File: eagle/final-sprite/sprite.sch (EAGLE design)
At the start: 60 parts, among them J1 M20-7910442R, U1 CC430F513X, U2 LSM9DS1, U4 DRV8837, U5 ADP5092, U6 DRV8837, U7 DRV8837, X1 SPRITEPIN_SPRITE_PIN, X2 SPRITEPIN_SPRITE_PIN

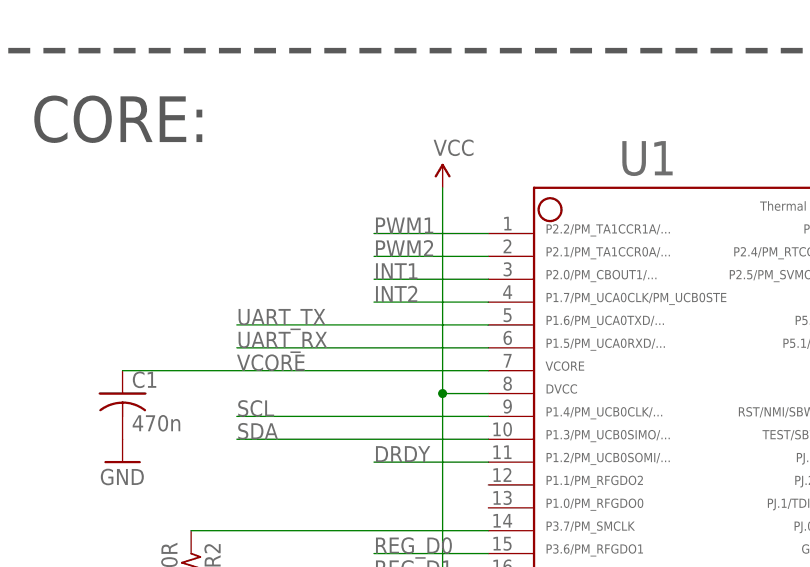
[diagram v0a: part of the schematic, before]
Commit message: routed some more routes
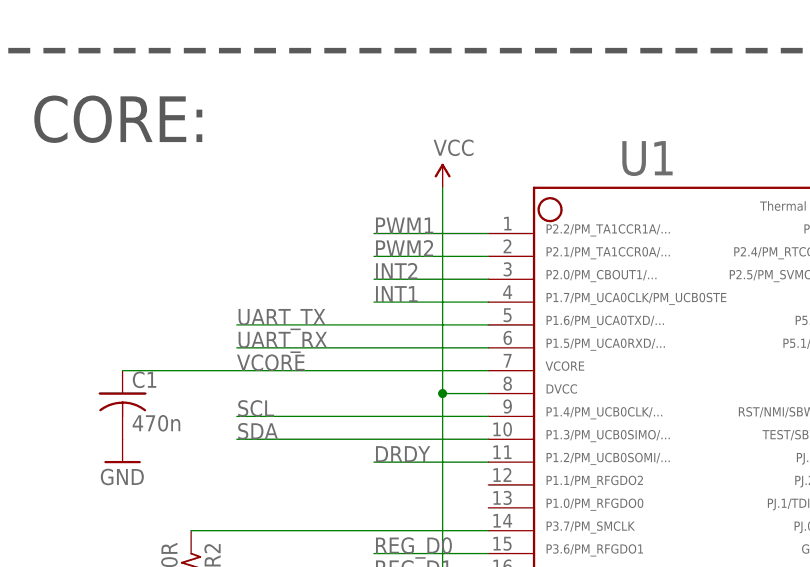
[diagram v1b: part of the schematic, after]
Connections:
- net INT1: now also U1.4; no longer U1.3
- net INT2: now also U1.3; no longer U1.4
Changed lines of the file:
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@@
 </segment>
 <segment>
-<wire x1="-20.32" y1="-193.04" x2="-33.02" y2="-193.04" width="0.1524" layer="91"/>
-<label x="-33.02" y="-193.04" size="1.778" layer="95"/>
-<pinref part="U1" gate="G$1" pin="3"/>
+<wire x1="-20.32" y1="-195.58" x2="-33.02" y2="-195.58" width="0.1524" layer="91"/>
+<label x="-33.02" y="-195.58" size="1.778" layer="95"/>
+<pinref part="U1" gate="G$1" pin="4"/>
 </segment>
 </net>
@@
 </segment>
 <segment>
-<wire x1="-20.32" y1="-195.58" x2="-33.02" y2="-195.58" width="0.1524" layer="91"/>
-<label x="-33.02" y="-195.58" size="1.778" layer="95"/>
-<pinref part="U1" gate="G$1" pin="4"/>
+<wire x1="-20.32" y1="-193.04" x2="-33.02" y2="-193.04" width="0.1524" layer="91"/>
+<label x="-33.02" y="-193.04" size="1.778" layer="95"/>
+<pinref part="U1" gate="G$1" pin="3"/>
 </segment>
 </net>

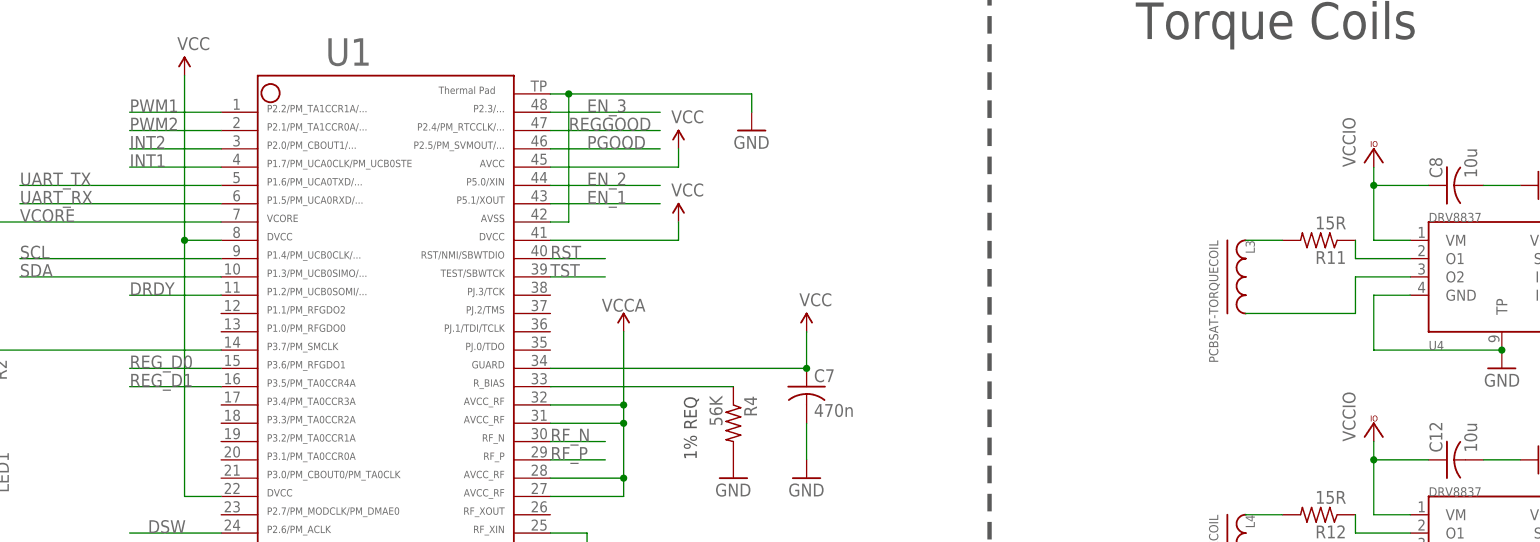
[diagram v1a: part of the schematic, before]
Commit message: routed all traces, need to do GND and VCC
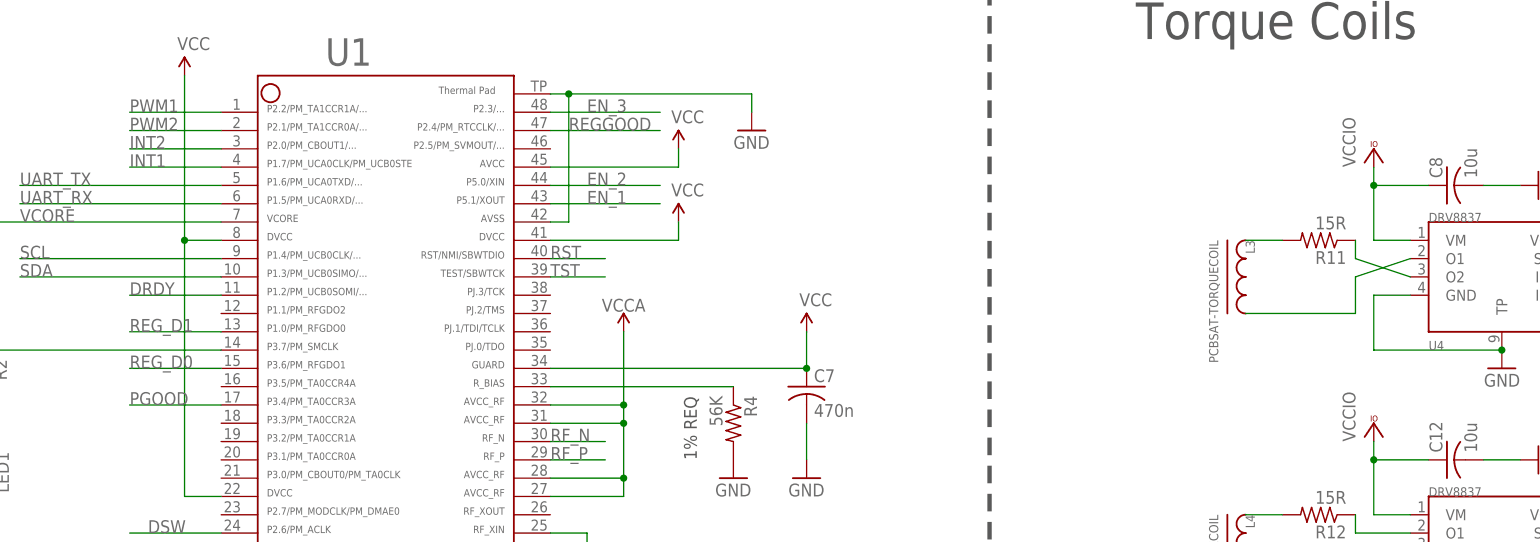
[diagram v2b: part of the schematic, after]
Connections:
- net N$14: now also U4.O1; no longer U4.O2
- net N$8: now also U4.O2; no longer U4.O1
- net PGOOD: now also U1.17; no longer U1.46
- net REG_D1: now also U1.13; no longer U1.16
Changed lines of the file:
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@@
 </segment>
 <segment>
-<wire x1="25.4" y1="-193.04" x2="40.64" y2="-193.04" width="0.1524" layer="91"/>
-<label x="30.48" y="-193.04" size="1.778" layer="95"/>
-<pinref part="U1" gate="G$1" pin="46"/>
+<pinref part="U1" gate="G$1" pin="17"/>
+<wire x1="-20.32" y1="-228.6" x2="-33.02" y2="-228.6" width="0.1524" layer="91"/>
+<label x="-33.02" y="-228.6" size="1.778" layer="95"/>
 </segment>
 </net>
@@
 </segment>
 <segment>
-<pinref part="U1" gate="G$1" pin="16"/>
-<wire x1="-20.32" y1="-226.06" x2="-33.02" y2="-226.06" width="0.1524" layer="91"/>
-<label x="-33.02" y="-226.06" size="1.778" layer="95"/>
+<pinref part="U1" gate="G$1" pin="13"/>
+<wire x1="-20.32" y1="-218.44" x2="-33.02" y2="-218.44" width="0.1524" layer="91"/>
+<label x="-33.02" y="-218.44" size="1.778" layer="95"/>
 </segment>
 </net>
@@
 <net name="N$8" class="0">
 <segment>
-<pinref part="U4" gate="G$1" pin="O1"/>
-<wire x1="144.78" y1="-208.28" x2="137.16" y2="-208.28" width="0.1524" layer="91"/>
+<pinref part="U4" gate="G$1" pin="O2"/>
+<wire x1="144.78" y1="-210.82" x2="137.16" y2="-208.28" width="0.1524" layer="91"/>
 <wire x1="137.16" y1="-205.74" x2="137.16" y2="-208.28" width="0.1524" layer="91"/>
 <pinref part="R11" gate="G$1" pin="1"/>
@@
 <net name="N$14" class="0">
 <segment>
-<pinref part="U4" gate="G$1" pin="O2"/>
-<wire x1="144.78" y1="-210.82" x2="137.16" y2="-210.82" width="0.1524" layer="91"/>
+<pinref part="U4" gate="G$1" pin="O1"/>
+<wire x1="144.78" y1="-208.28" x2="137.16" y2="-210.82" width="0.1524" layer="91"/>
 <wire x1="137.16" y1="-210.82" x2="137.16" y2="-215.9" width="0.1524" layer="91"/>
 <wire x1="137.16" y1="-215.9" x2="121.92" y2="-215.9" width="0.1524" layer="91"/>

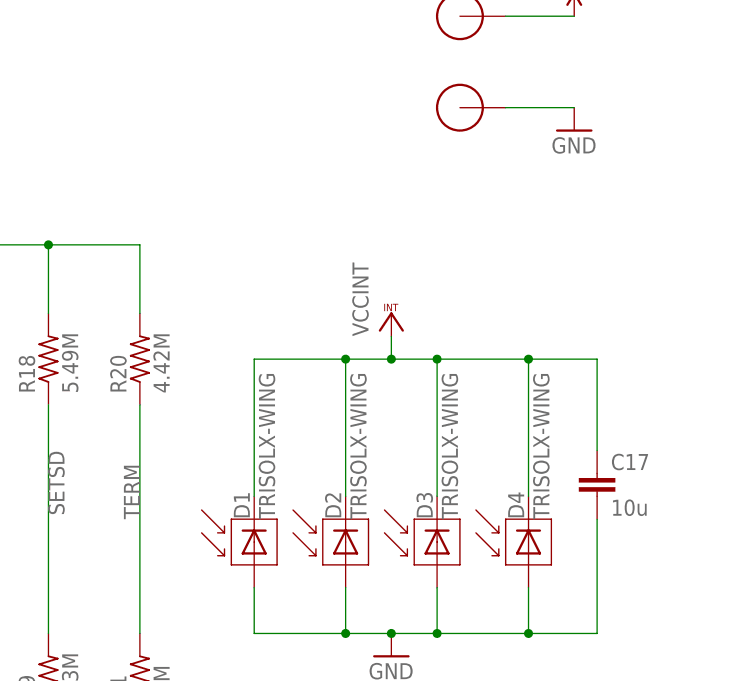
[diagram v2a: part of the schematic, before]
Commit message: added new trisol footprint to layout
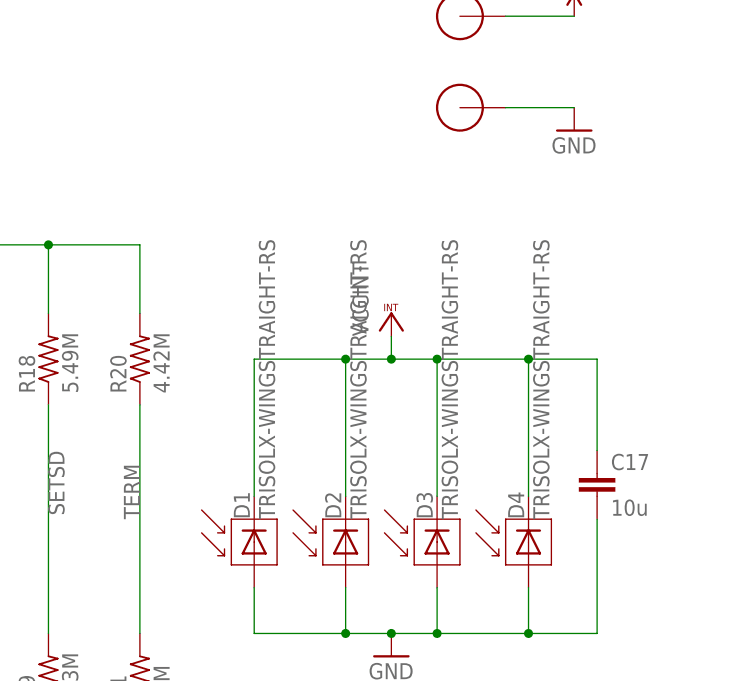
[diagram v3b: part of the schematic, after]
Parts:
- D1, D2, D3, D4: value TRISOLX-WING -> TRISOLX-WINGSTRAIGHT-RS; device STAC:TRISOLX-WING -> STAC:TRISOLX-WINGSTRAIGHT-RS
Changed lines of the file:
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@@
 <part name="X2" library="STAC" deviceset="SPRITEPIN_SPRITE_PIN" device=""/>
 <part name="B1" library="STAC" deviceset="UMAC_UMAC" device=""/>
-<part name="D1" library="STAC" deviceset="TRISOLX-WING" device=""/>
-<part name="D2" library="STAC" deviceset="TRISOLX-WING" device=""/>
-<part name="D3" library="STAC" deviceset="TRISOLX-WING" device=""/>
-<part name="D4" library="STAC" deviceset="TRISOLX-WING" device=""/>
+<part name="D2" library="STAC" deviceset="TRISOLX-WING" device="STRAIGHT-RS" value="TRISOLX-WINGSTRAIGHT-RS"/>
+<part name="D3" library="STAC" deviceset="TRISOLX-WING" device="STRAIGHT-RS" value="TRISOLX-WINGSTRAIGHT-RS"/>
+<part name="D4" library="STAC" deviceset="TRISOLX-WING" device="STRAIGHT-RS" value="TRISOLX-WINGSTRAIGHT-RS"/>
 <part name="U3" library="STAC" deviceset="SPRITETCXO_TCXO_7Z" device=""/>
 <part name="U1" library="STAC" deviceset="CC430F513X" device=""/>
@@
 <part name="L3" library="STAC" deviceset="PCBSAT-TORQUECOIL" device=""/>
 <part name="L4" library="STAC" deviceset="PCBSAT-TORQUECOIL" device=""/>
+<part name="D1" library="STAC" deviceset="TRISOLX-WING" device="STRAIGHT-RS" value="TRISOLX-WINGSTRAIGHT-RS"/>
 </parts>
 <sheets>
@@
 <instance part="X2" gate="G$1" x="279.4" y="-83.82"/>
 <instance part="B1" gate="G$1" x="175.26" y="-134.62"/>
-<instance part="D1" gate="G$1" x="256.54" y="-132.08" rot="R90"/>
 <instance part="D2" gate="G$1" x="266.7" y="-132.08" rot="R90"/>
 <instance part="D3" gate="G$1" x="276.86" y="-132.08" rot="R90"/>
@@
 <instance part="L3" gate="G$1" x="121.92" y="-210.82" rot="R270"/>
 <instance part="L4" gate="G$1" x="121.92" y="-248.92" rot="R270"/>
+<instance part="D1" gate="G$1" x="256.54" y="-132.08" rot="R90"/>
 </instances>
 <busses>
@@
 <wire x1="294.64" y1="-142.24" x2="287.02" y2="-142.24" width="0.1524" layer="91"/>
 <junction x="287.02" y="-142.24"/>
-<pinref part="D1" gate="G$1" pin="A"/>
 <pinref part="D2" gate="G$1" pin="A"/>
 <pinref part="D3" gate="G$1" pin="A"/>
 <pinref part="D4" gate="G$1" pin="A"/>
+<pinref part="D1" gate="G$1" pin="A"/>
 </segment>
 <segment>
@@
 <wire x1="294.64" y1="-111.76" x2="287.02" y2="-111.76" width="0.1524" layer="91"/>
 <junction x="287.02" y="-111.76"/>
-<pinref part="D1" gate="G$1" pin="C"/>
 <pinref part="D2" gate="G$1" pin="C"/>
 <pinref part="D3" gate="G$1" pin="C"/>
 <pinref part="D4" gate="G$1" pin="C"/>
-</segment>
-<segment>
+<pinref part="D1" gate="G$1" pin="C"/>
+</segment>
+<segment>
